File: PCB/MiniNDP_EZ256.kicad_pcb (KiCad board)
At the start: 2 copper layers, 60 x 34 mm, 18 parts, among them J1 Conn_02x20_Odd_Even, U1 HC238, U2 HC4040, U3 HC573, U4 AS6C2008A

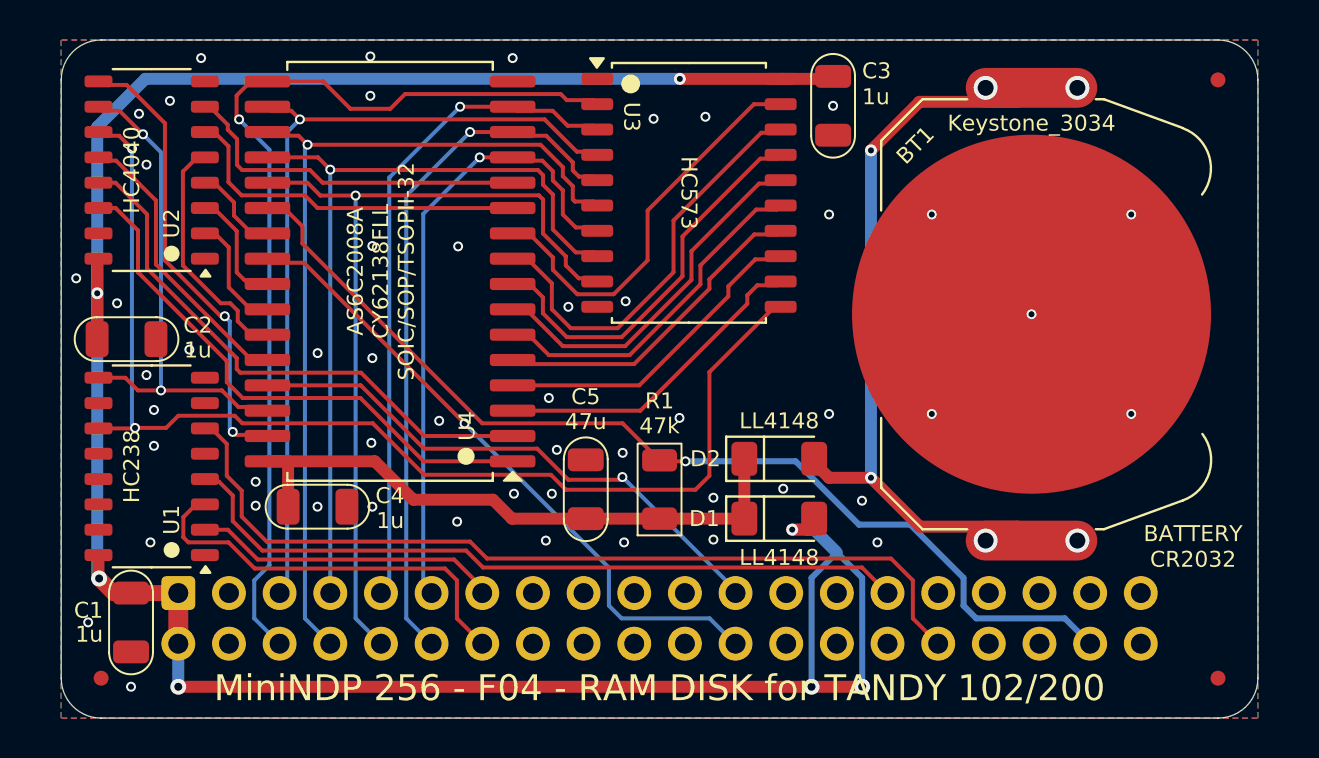
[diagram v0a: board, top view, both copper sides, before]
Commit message: rename 256_F to EZ256
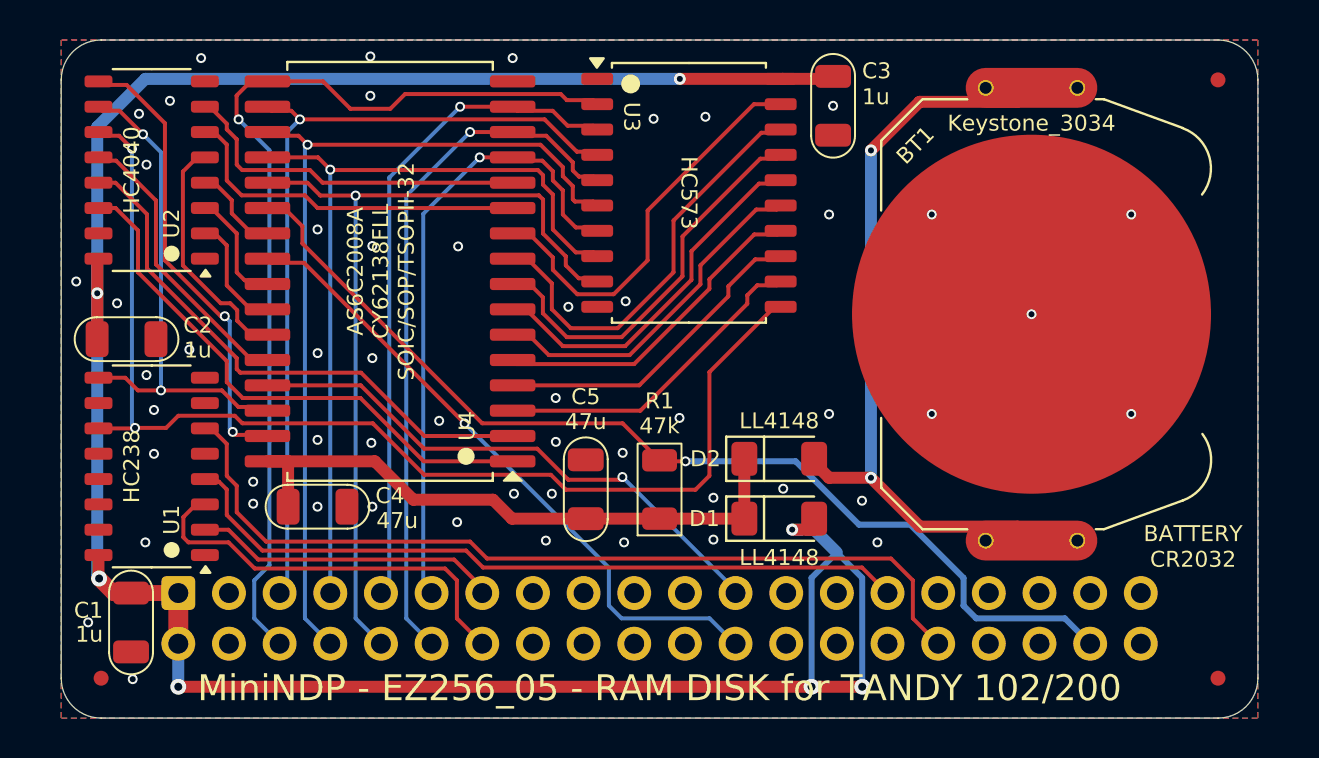
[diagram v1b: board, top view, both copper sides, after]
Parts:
- added REF**: pth_nail, 000_LOCAL:pth_nail, F.Cu at (172.9, 88.4)
- added REF**: pth_nail, 000_LOCAL:pth_nail, F.Cu at (172.9, 111.1)
- added REF**: pth_nail, 000_LOCAL:pth_nail, F.Cu at (168.3, 88.4)
- added REF**: pth_nail, 000_LOCAL:pth_nail, F.Cu at (168.3, 111.1)
- C4: value 1u -> 47u
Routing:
- net GND: vias 52 -> 54
- net +BATT: vias 6 -> 2
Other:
- board text added: "block0-255: OUT 129,N read byte: N=INP(131) write byte: OUT 131,N"

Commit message: embed code font in pcb, bom export filename variables, delete extra battery trace
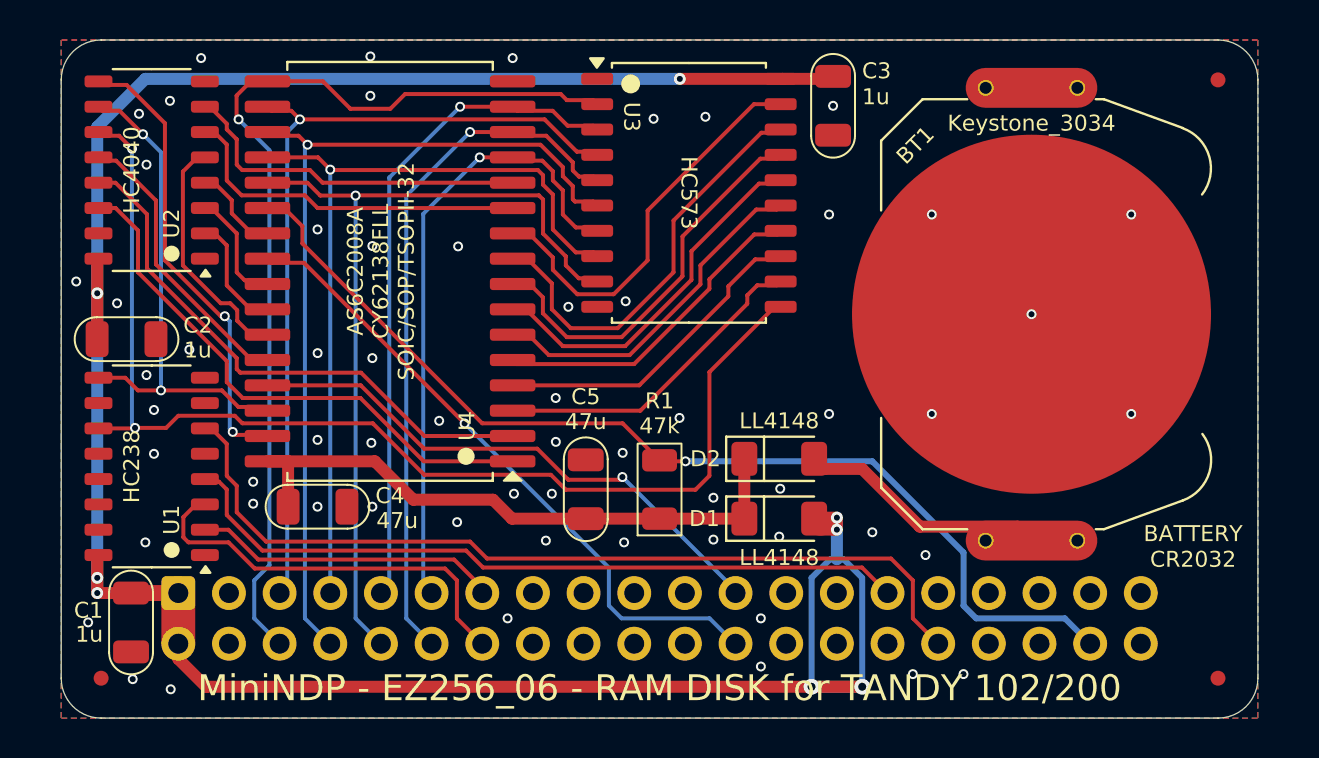
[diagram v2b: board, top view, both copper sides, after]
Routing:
- net +BATT: track 38.5 -> 12.6 mm, vias 2 -> 0
- net /RAMRST: track 51.6 -> 52.4 mm
- net VBUS: track 128.0 -> 128.4 mm, vias 7 -> 8
- net GND: vias 54 -> 61
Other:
- board text removed: "Install the font in the font directory for the BASIC code."
